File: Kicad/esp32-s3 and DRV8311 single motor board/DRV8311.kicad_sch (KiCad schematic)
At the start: 11 parts, among them J3 Molex_PicoBlade_53048-0310 Ho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, U2 DRV8311HRRWR

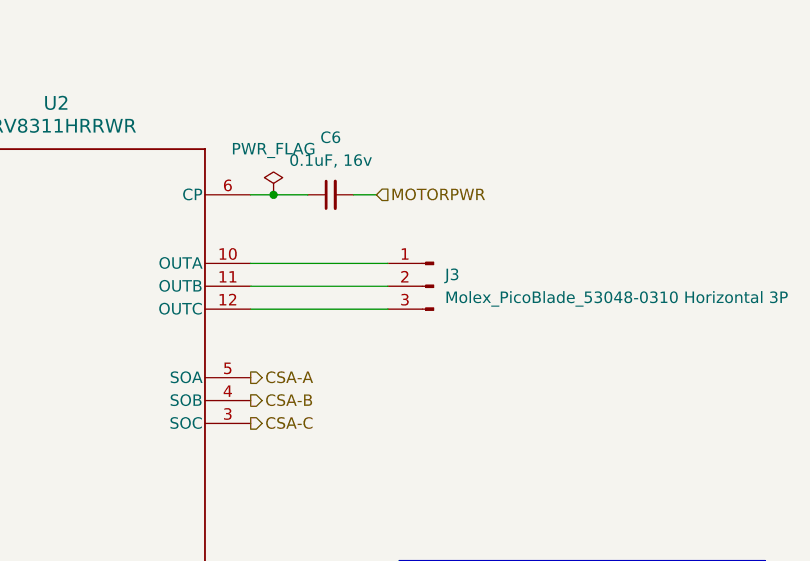
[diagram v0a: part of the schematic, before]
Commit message: Wiring some signal wires and moving power around to accomodate
There are location conflicts left and right! I will eventually get this mess sorted out, but I am wondering about 6 layer boards and blind vias. 4 layers will keep the costs down though!
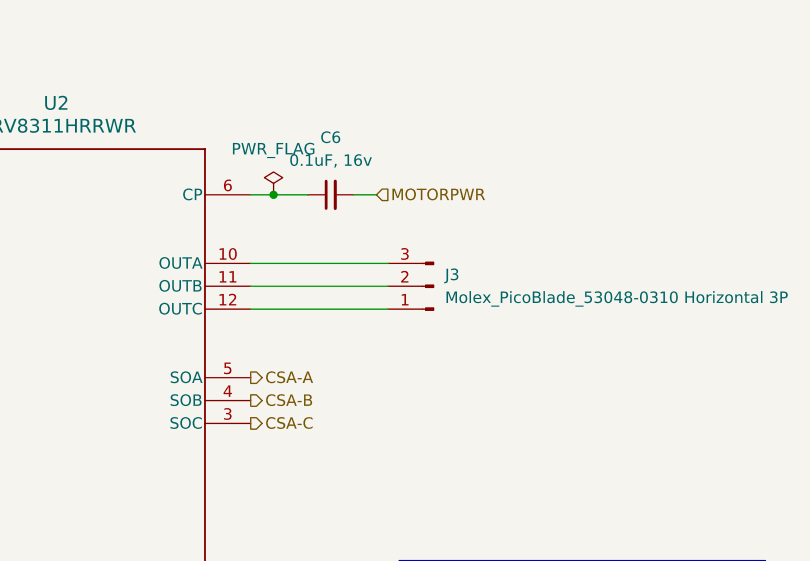
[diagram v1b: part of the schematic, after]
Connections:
- net at U2.10 (OUTA): now also J3.3 (Pin_3); no longer J3.1 (Pin_1)
- net at U2.12 (OUTC): now also J3.1 (Pin_1); no longer J3.3 (Pin_3)

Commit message: Routing test pads & power
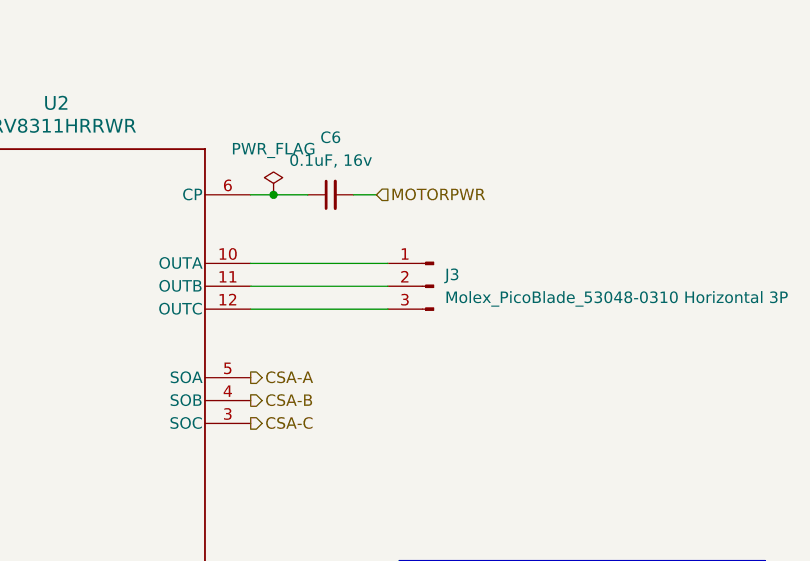
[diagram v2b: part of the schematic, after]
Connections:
- net at U2.10 (OUTA): now also J3.1 (Pin_1); no longer J3.3 (Pin_3)
- net at U2.12 (OUTC): now also J3.3 (Pin_3); no longer J3.1 (Pin_1)
